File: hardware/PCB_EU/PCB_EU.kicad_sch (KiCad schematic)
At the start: 0 parts

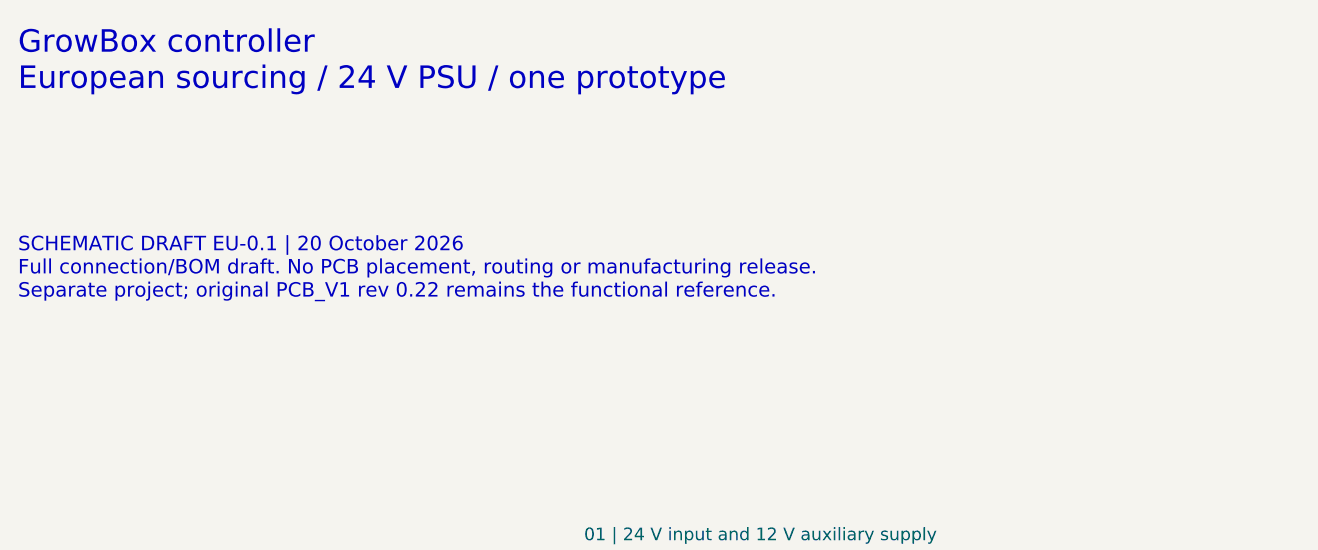
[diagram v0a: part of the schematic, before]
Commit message: hardware: add EU 100x100 unrouted placement and native PCB validation
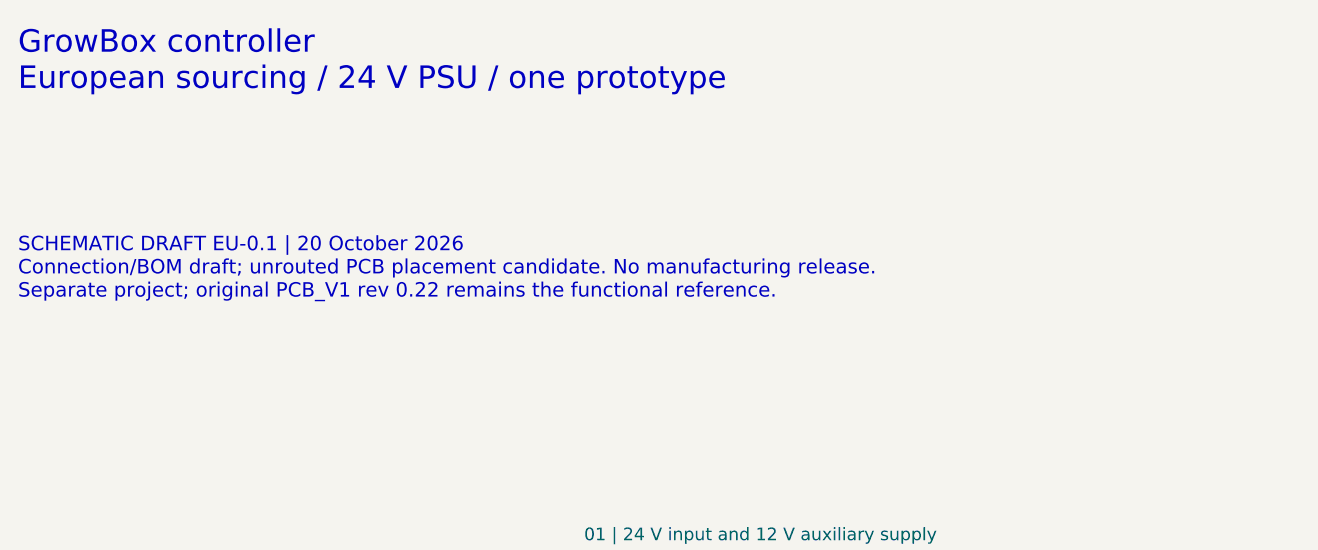
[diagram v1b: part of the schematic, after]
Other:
- note added: "SCHEMATIC DRAFT EU-0.1 | 20 October 2026 Connection/BOM draft; unrouted PCB placement candidate. No manufacturing release. Separate project; original PCB_V1 rev 0.22 remains the functional reference."
- note removed: "SCHEMATIC DRAFT EU-0.1 | 20 October 2026 Full connection/BOM draft. No PCB placement, routing or manufacturing release. Separate project; original PCB_V1 rev 0.22 remains the functional reference."
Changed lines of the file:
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@@
-(kicad_sch (version 20260306) (generator "eeschema") (generator_version "10.0") (paper "A3") (title_block (title "GrowBox | EU redesign | schematic review") (date "2026-10-20") (rev "EU-0.1") (company "GrowBox | EU prototype") (comment 1 "SCHEMATIC DRAFT | no PCB / manufacturing release"))
+(kicad_sch (version 20260306) (generator "eeschema") (generator_version "10.0") (paper "A3") (title_block (title "GrowBox | EU redesign | schematic review") (date "2026-10-20") (rev "EU-0.1") (company "GrowBox | EU prototype") (comment 1 "SCHEMATIC DRAFT | UNROUTED PCB | no manufacturing release"))
 (text "GrowBox controller\nEuropean sourcing / 24 V PSU / one prototype" (at 20 17 0) (effects (font (size 2.5 2.5)) (justify left top)))
-(text "SCHEMATIC DRAFT EU-0.1 | 20 October 2026\nFull connection/BOM draft. No PCB placement, routing or manufacturing release.\nSeparate project; original PCB_V1 rev 0.22 remains the functional reference." (at 20 40 0) (effects (font (size 1.6 1.6)) (justify left top)))
+(text "SCHEMATIC DRAFT EU-0.1 | 20 October 2026\nConnection/BOM draft; unrouted PCB placement candidate. No manufacturing release.\nSeparate project; original PCB_V1 rev 0.22 remains the functional reference." (at 20 40 0) (effects (font (size 1.6 1.6)) (justify left top)))
 (sheet (at 25 75) (size 155 28) (stroke (width 0.254) (type default)) (fill (color 0 0 0 0)) (property "Sheetname" "01 | 24 V input and 12 V auxiliary supply" (at 102.5 73 0) (effects (font (size 1.4 1.4)) )) (property "Sheetfile" "InputPower.kicad_sch" (at 102.5 105 0) (effects (font (size 1 1)) )) (instances (project "PCB_EU" (path "/06532805-118c-508c-83b1-07900809d479" (page "2")))))
 (sheet (at 210 75) (size 155 28) (stroke (width 0.254) (type default)) (fill (color 0 0 0 0)) (property "Sheetname" "02 | 3.3 V supply and ESP32" (at 287.5 73 0) (effects (font (size 1.4 1.4)) )) (property "Sheetfile" "MCU.kicad_sch" (at 287.5 105 0) (effects (font (size 1 1)) )) (instances (project "PCB_EU" (path "/06532805-118c-508c-83b1-07900809d479" (page "3")))))

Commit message: Route initial EU LED1 power connections and add native copper checks
Improve LED1 placement without changing the electrical BOM. Add 40 track segments, 8 vias and an In1 GND plane; verify eight physical copper groups. Keep 361 remaining connections and all mechanical, ampacity and firmware limitations explicit.
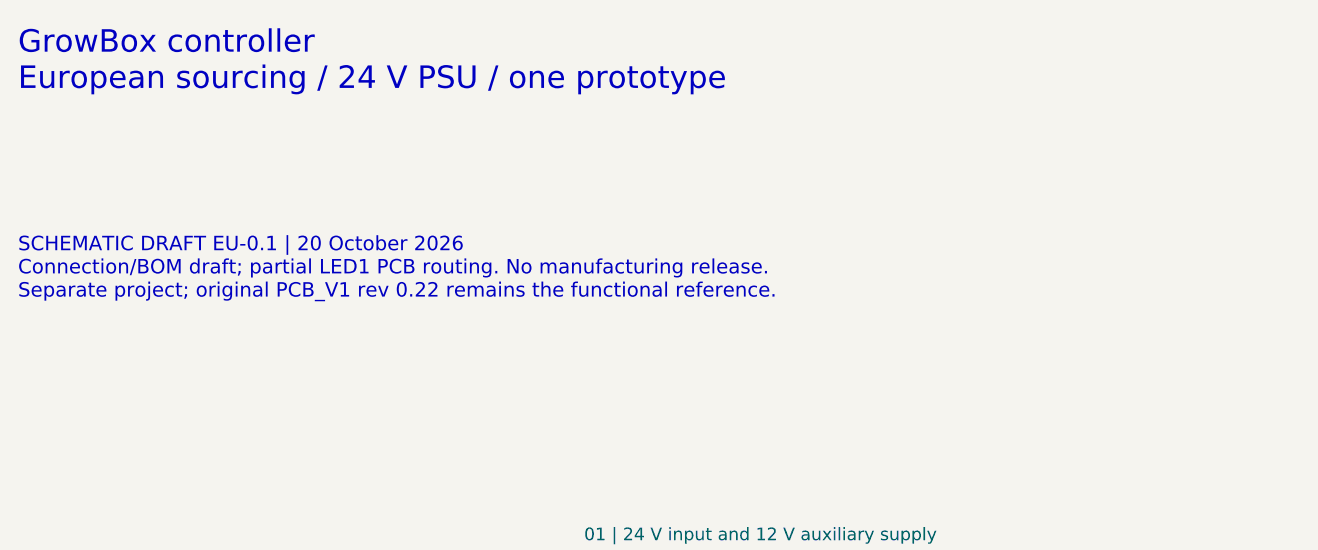
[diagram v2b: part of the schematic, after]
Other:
- note added: "SCHEMATIC DRAFT EU-0.1 | 20 October 2026 Connection/BOM draft; partial LED1 PCB routing. No manufacturing release. Separate project; original PCB_V1 rev 0.22 remains the functional reference."
- note removed: "SCHEMATIC DRAFT EU-0.1 | 20 October 2026 Connection/BOM draft; unrouted PCB placement candidate. No manufacturing release. Separate project; original PCB_V1 rev 0.22 remains the functional reference."
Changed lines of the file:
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@@
-(kicad_sch (version 20260306) (generator "eeschema") (generator_version "10.0") (paper "A3") (title_block (title "GrowBox | EU redesign | schematic review") (date "2026-10-20") (rev "EU-0.1") (company "GrowBox | EU prototype") (comment 1 "SCHEMATIC DRAFT | UNROUTED PCB | no manufacturing release"))
+(kicad_sch (version 20260306) (generator "eeschema") (generator_version "10.0") (paper "A3") (title_block (title "GrowBox | EU redesign | schematic review") (date "2026-10-20") (rev "EU-0.1") (company "GrowBox | EU prototype") (comment 1 "SCHEMATIC DRAFT | PARTIAL LED1 PCB ROUTING | no manufacturing release"))
 (text "GrowBox controller\nEuropean sourcing / 24 V PSU / one prototype" (at 20 17 0) (effects (font (size 2.5 2.5)) (justify left top)))
-(text "SCHEMATIC DRAFT EU-0.1 | 20 October 2026\nConnection/BOM draft; unrouted PCB placement candidate. No manufacturing release.\nSeparate project; original PCB_V1 rev 0.22 remains the functional reference." (at 20 40 0) (effects (font (size 1.6 1.6)) (justify left top)))
+(text "SCHEMATIC DRAFT EU-0.1 | 20 October 2026\nConnection/BOM draft; partial LED1 PCB routing. No manufacturing release.\nSeparate project; original PCB_V1 rev 0.22 remains the functional reference." (at 20 40 0) (effects (font (size 1.6 1.6)) (justify left top)))
 (sheet (at 25 75) (size 155 28) (stroke (width 0.254) (type default)) (fill (color 0 0 0 0)) (property "Sheetname" "01 | 24 V input and 12 V auxiliary supply" (at 102.5 73 0) (effects (font (size 1.4 1.4)) )) (property "Sheetfile" "InputPower.kicad_sch" (at 102.5 105 0) (effects (font (size 1 1)) )) (instances (project "PCB_EU" (path "/06532805-118c-508c-83b1-07900809d479" (page "2")))))
 (sheet (at 210 75) (size 155 28) (stroke (width 0.254) (type default)) (fill (color 0 0 0 0)) (property "Sheetname" "02 | 3.3 V supply and ESP32" (at 287.5 73 0) (effects (font (size 1.4 1.4)) )) (property "Sheetfile" "MCU.kicad_sch" (at 287.5 105 0) (effects (font (size 1 1)) )) (instances (project "PCB_EU" (path "/06532805-118c-508c-83b1-07900809d479" (page "3")))))
